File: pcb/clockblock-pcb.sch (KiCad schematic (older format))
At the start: 115 parts, among them IC1 TLC5971, IC2 TLC5971, IC3 TLC5971, IC4 PCF2129AT, IC5 TLV71333, IC6 ATTINY167, IC7 FT230X, J2 USB, P13 USBtoMAIN, P14 AVR_ISP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

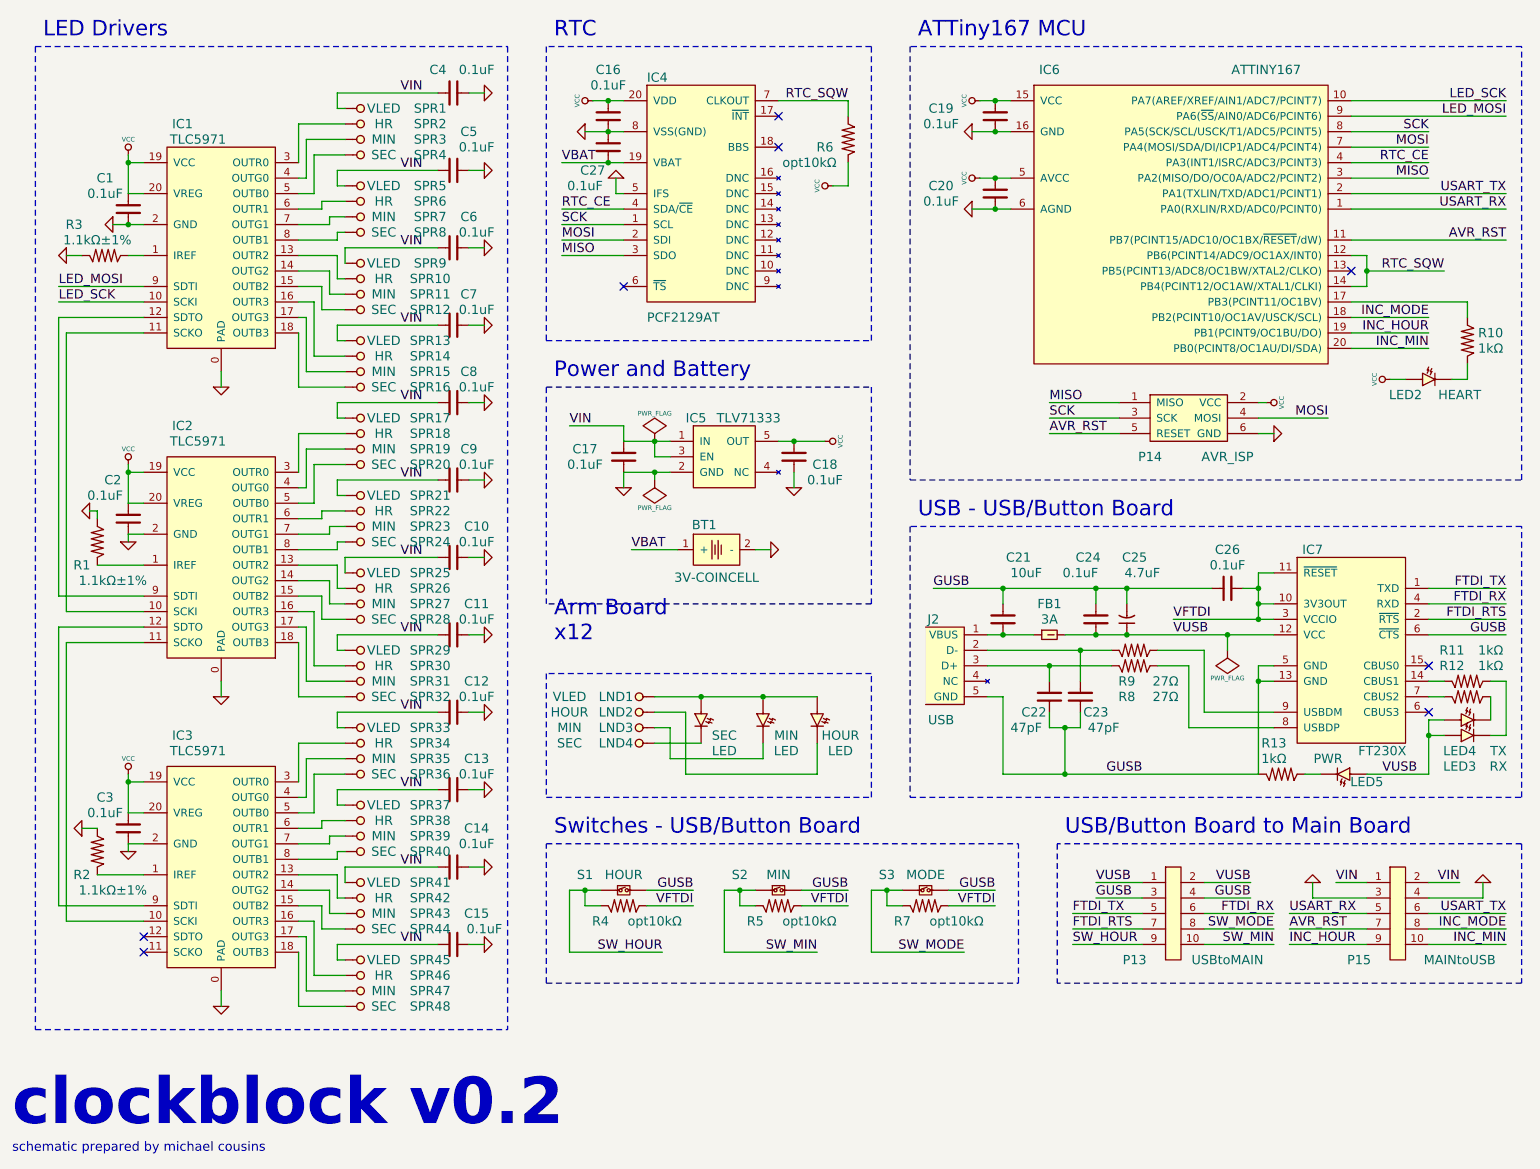
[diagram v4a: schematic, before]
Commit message: 10k pullups are no longer labeled as optional
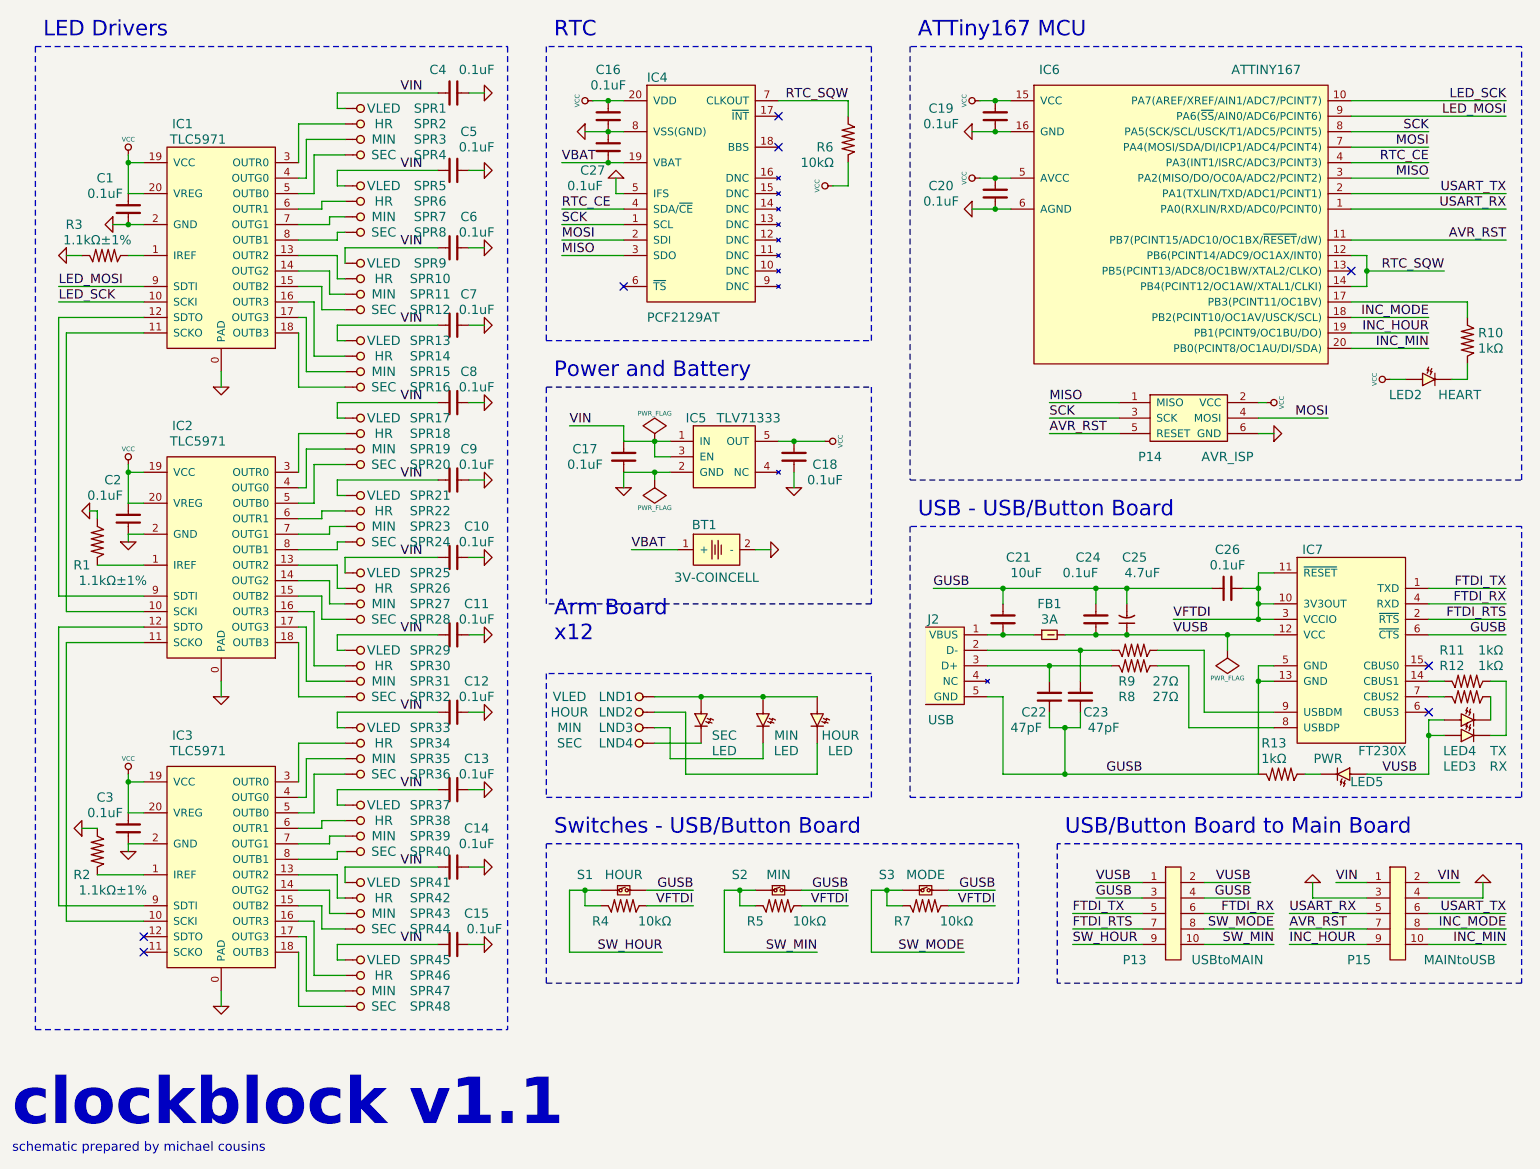
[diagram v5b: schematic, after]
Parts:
- R4, R5, R6, R7: value opt10kΩ -> 10kΩ
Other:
- note added: "clockblock v1.1"
- note removed: "clockblock v0.2"
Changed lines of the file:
@@
 Title "clockblock pcb"
 Date "2 jan 2014"
-Rev "0.2"
+Rev "1.1"
 Comp "Wiley Cousins, LLC."
 Comment1 "released under the terms of the Creative Commons Attribution Share-Alike 3.0 license"
@@
 $EndComp
 Text Notes 550  7800 0    300  ~ 60
-clockblock v0.2
+clockblock v1.1
 $Comp
 L PCF2129AT IC4
@@
 P 5950 1400
 F 0 "R6" V 5900 1550 60  0000 C CNN
-F 1 "opt10kΩ" V 5800 1650 60  0000 C CNN
+F 1 "10kΩ" V 5800 1600 60  0000 C CNN
 F 2 "0603(1608m)" H 5950 1400 60  0001 C CNN
 F 3 "~" H 5950 1400 60  0001 C CNN
@@
 P 4500 6350
 F 0 "R4" H 4350 6250 60  0000 C CNN
-F 1 "opt10kΩ" H 4700 6250 60  0000 C CNN
+F 1 "10kΩ" H 4700 6250 60  0000 C CNN
 F 2 "0603(1608m)" H 4500 6350 60  0001 C CNN
 F 3 "~" H 4500 6350 60  0001 C CNN
@@
 P 5500 6350
 F 0 "R5" H 5350 6250 60  0000 C CNN
-F 1 "opt10kΩ" H 5700 6250 60  0000 C CNN
+F 1 "10kΩ" H 5700 6250 60  0000 C CNN
 F 2 "0603(1608m)" H 5500 6350 60  0001 C CNN
 F 3 "~" H 5500 6350 60  0001 C CNN
@@
 P 6450 6350
 F 0 "R7" H 6300 6250 60  0000 C CNN
-F 1 "opt10kΩ" H 6650 6250 60  0000 C CNN
+F 1 "10kΩ" H 6650 6250 60  0000 C CNN
 F 2 "0603(1608m)" H 6450 6350 60  0001 C CNN
 F 3 "~" H 6450 6350 60  0001 C CNN
@@
 E1 7A 30 2F E3 9E BF BB FC D0 5C 2F 77 12 1D A4 F0 58 02 39 97 10 5D 3F 53 4D 5C E7 C1 2F 96 BB
 0B B8 4B 44 66 C0 DD 9B E5 70 E1 99 33 E3 22 76 A6 C0 F5 70 86 E1 7A 3C 1F 00 F7 E2 62 F9 87 B5
-4B 6B 3B F8 7F 51 4C 22 23 01 FF ED 6E 00 00 00 00 49 45 4E 44 AE 42 60 82 15 $EndBitmap
+4B 6B 3B F8 7F 51 4C 22 23 01 FF ED 6E 00 00 00 00 49 45 4E 44 AE 42 60 82 0D $EndBitmap
 EndData
 $EndBitmap
@@
 00 00 80 1C 90 88 03 00 00 00 00 00 00 72 40 22 0E 00 00 00 00 00 00 C8 01 89 38 00 00 00 00 00
 00 20 07 24 E2 00 00 00 00 00 00 80 1C FC FF 3E 6A 41 A6 FA 5D A5 94 00 00 00 00 49 45 4E 44 AE
-42 60 82 79 $EndBitmap
+42 60 82 9A $EndBitmap
 EndData
 $EndBitmap

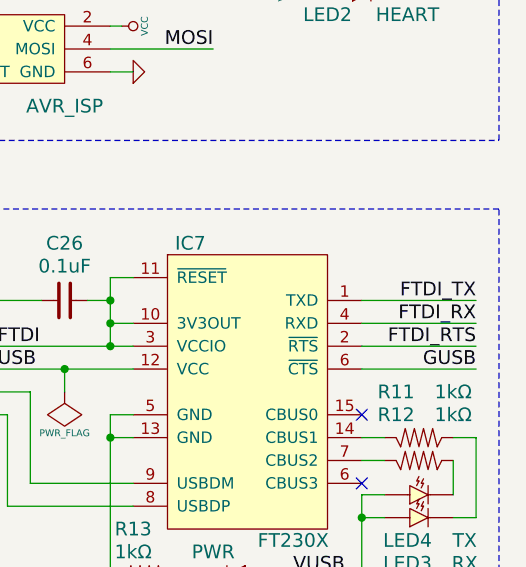
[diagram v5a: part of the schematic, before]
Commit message: added a capicitor the the FTDI RTS line. fixes #6
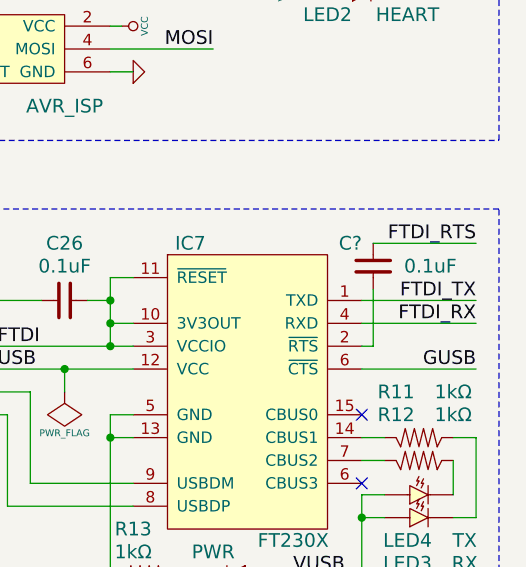
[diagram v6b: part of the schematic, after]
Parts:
- added C?: 0.1uF, ~, symbol C
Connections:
- net FTDI_RTS: now also C?.2; no longer IC7.2 (~RTS~)
- new net: C?.1, IC7.2 (~RTS~)
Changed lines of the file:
@@
 Text Label 10200 4400 2    60   ~ 0
 FTDI_RX
-Text Label 10200 4500 2    60   ~ 0
+Text Label 10200 4050 2    60   ~ 0
 FTDI_RTS
 $Comp
@@
 E1 7A 30 2F E3 9E BF BB FC D0 5C 2F 77 12 1D A4 F0 58 02 39 97 10 5D 3F 53 4D 5C E7 C1 2F 96 BB
 0B B8 4B 44 66 C0 DD 9B E5 70 E1 99 33 E3 22 76 A6 C0 F5 70 86 E1 7A 3C 1F 00 F7 E2 62 F9 87 B5
-4B 6B 3B F8 7F 51 4C 22 23 01 FF ED 6E 00 00 00 00 49 45 4E 44 AE 42 60 82 0D $EndBitmap
+4B 6B 3B F8 7F 51 4C 22 23 01 FF ED 6E 00 00 00 00 49 45 4E 44 AE 42 60 82 11 $EndBitmap
 EndData
 $EndBitmap
@@
 00 00 80 1C 90 88 03 00 00 00 00 00 00 72 40 22 0E 00 00 00 00 00 00 C8 01 89 38 00 00 00 00 00
 00 20 07 24 E2 00 00 00 00 00 00 80 1C FC FF 3E 6A 41 A6 FA 5D A5 94 00 00 00 00 49 45 4E 44 AE
-42 60 82 9A $EndBitmap
+42 60 82 80 $EndBitmap
 EndData
 $EndBitmap
@@
 	10200 4400 9700 4400
 Wire Wire Line
-	10200 4500 9700 4500
-Wire Wire Line
 	9800 5000 9700 5000
 Wire Wire Line
@@
 Wire Notes Line
 	4000 5650 6100 5650
+$Comp
+L C C?
+U 1 1 52C5F0C4
+P 9750 4150
+F 0 "C?" V 9850 4250 60  0000 C CNN
+F 1 "0.1uF" V 9750 3900 60  0000 C CNN
+F 2 "~" H 9750 4150 60  0001 C CNN
+F 3 "~" H 9750 4150 60  0001 C CNN
+	1    9750 4150
+	0    -1   -1   0
+$EndComp
+Wire Wire Line
+	9700 4500 9750 4500
+Wire Wire Line
+	9750 4500 9750 4250
+Wire Wire Line
+	9750 4050 10200 4050
 $EndSCHEMATC

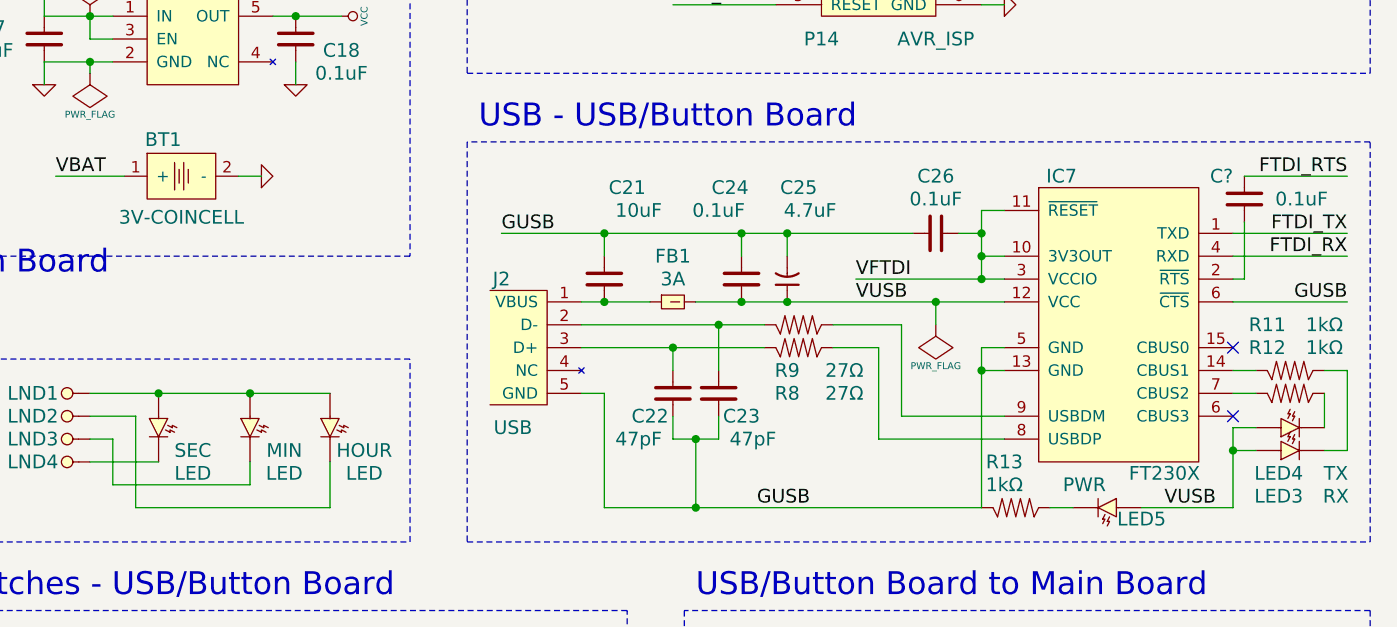
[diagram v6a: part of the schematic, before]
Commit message: fixed up layout issues related to schematic fixes
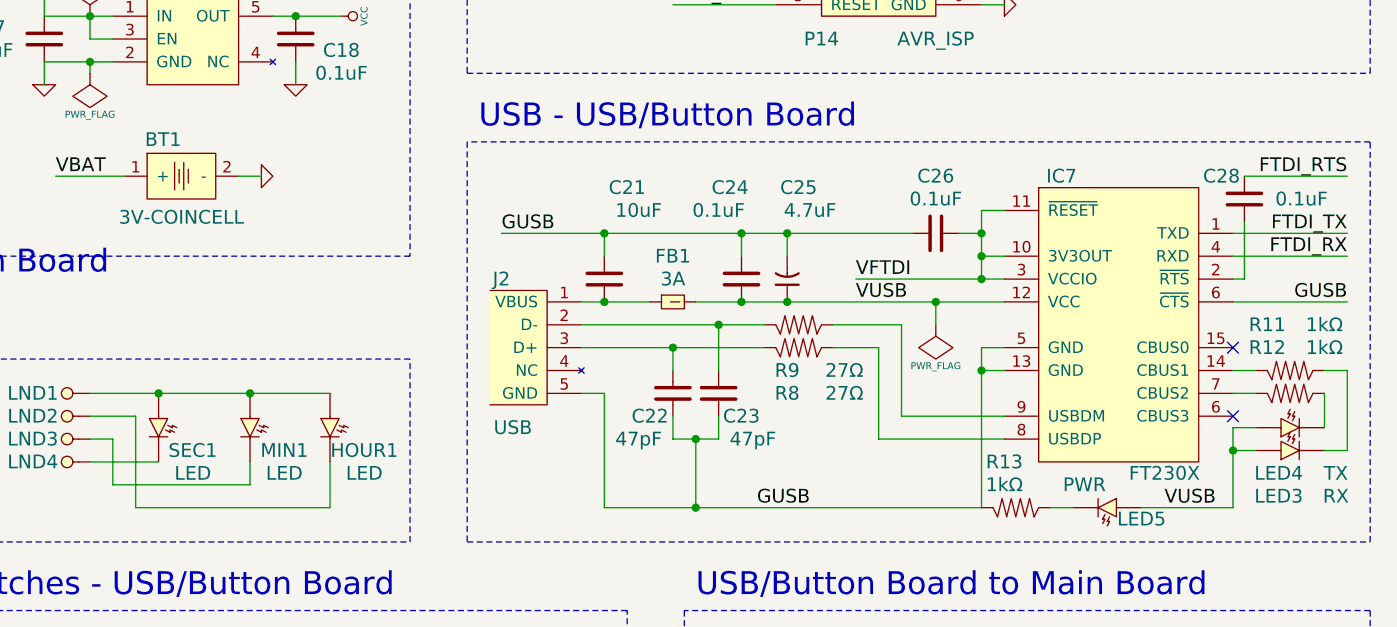
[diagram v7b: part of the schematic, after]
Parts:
- gave numbers to parts that had none: 1
- renumbered HOUR to HOUR1, MIN to MIN1, SEC to SEC1
